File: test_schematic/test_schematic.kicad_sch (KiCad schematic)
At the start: 13 parts, among them SW1 SW_Push, SW2 SW_Push, SW3 SW_Push, SW4 SW_Push, U1 MCP4251-103E/P, U2 ESP32-S3, U3 MCP4251-103E/P

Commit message: Update test_schematic.kicad_sch
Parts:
- added SW5, SW6: SW_SPDT, symbol Switch:SW_SPDT
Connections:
- net at U2.14 (GPIO9): now also SW5.1 (A)
- net at U2.15 (GPIO10): now also SW5.3 (C)
- net at U2.16 (GPIO11): now also SW6.1 (A)
- net at U2.17 (GPIO12): now also SW6.3 (C)

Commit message: Update test_schematic.kicad_sch
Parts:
- added LS1: Speaker, symbol Device:Speaker
- added MK1: SPH0645LM4H, Sensor_Audio:Knowles_SPH0645LM4H-6_3.5x2.65mm, symbol Sensor_Audio:SPH0645LM4H
- added U4: MAX98357A, Package_DFN_QFN:TQFN-16-1EP_3x3mm_P0.5mm_EP1.23x1.23mm, symbol Audio:MAX98357A
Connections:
- new net: LS1.1, U4.9 (OUTP)
- new net: LS1.2, U4.10 (OUTN)
- new net: U4.11 (GND), U4.15 (GND), U4.3 (GND)
- new net: U4.7 (VDD), U4.8 (VDD)
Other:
- note added: "Amplifier"
- note added: "Microphone"
- moved on the sheet: C1, C2, C3, C4, C5, C6, SW1, SW2, SW3, SW4, SW5, SW6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

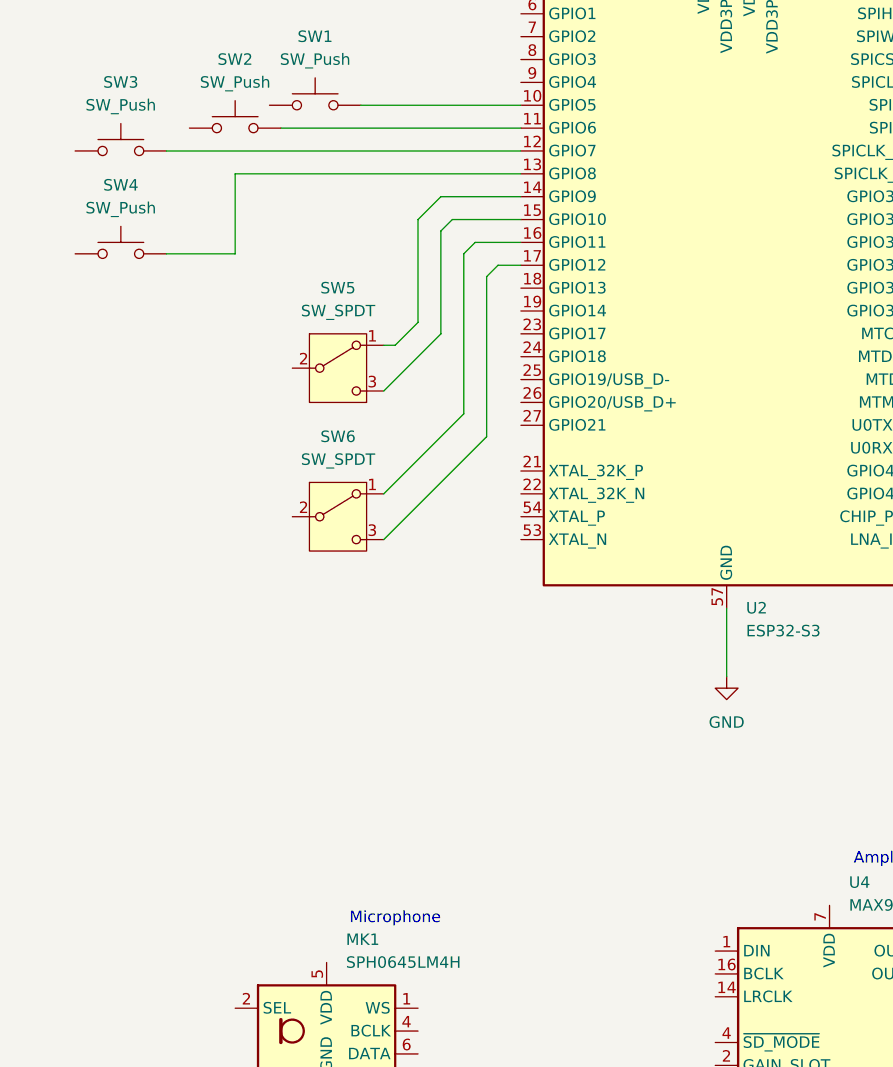
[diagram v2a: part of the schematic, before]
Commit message: Update test schematic
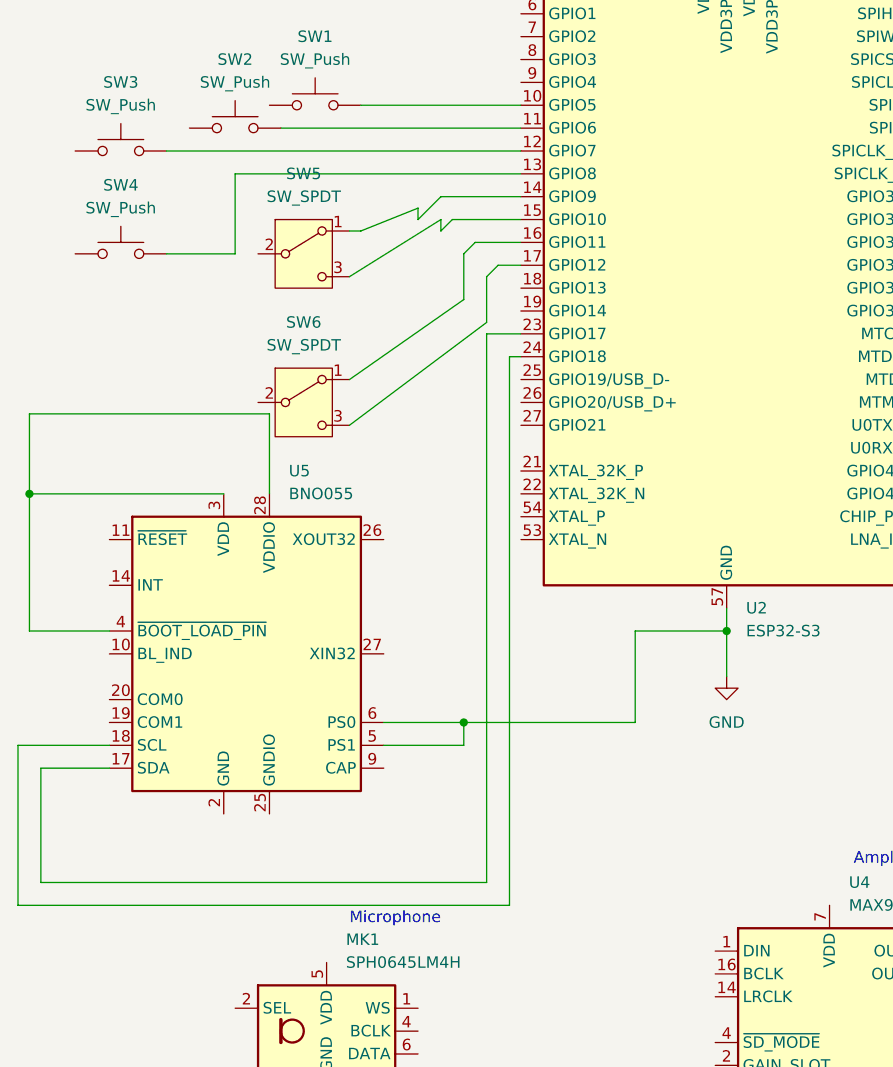
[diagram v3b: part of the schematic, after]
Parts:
- added U5: BNO055, Package_LGA:LGA-28_5.2x3.8mm_P0.5mm, symbol Sensor_Motion:BNO055
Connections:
- net GND: now also U5.5 (PS1), U5.6 (PS0)
- net at U2.23 (GPIO17): now also U5.17 (SDA)
- net at U2.24 (GPIO18): now also U5.18 (SCL)
- new net: U5.28 (VDDIO), U5.3 (VDD), U5.4 (~{BOOT_LOAD_PIN})
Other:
- moved on the sheet: SW5, SW6
